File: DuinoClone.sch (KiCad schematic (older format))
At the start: 13 parts

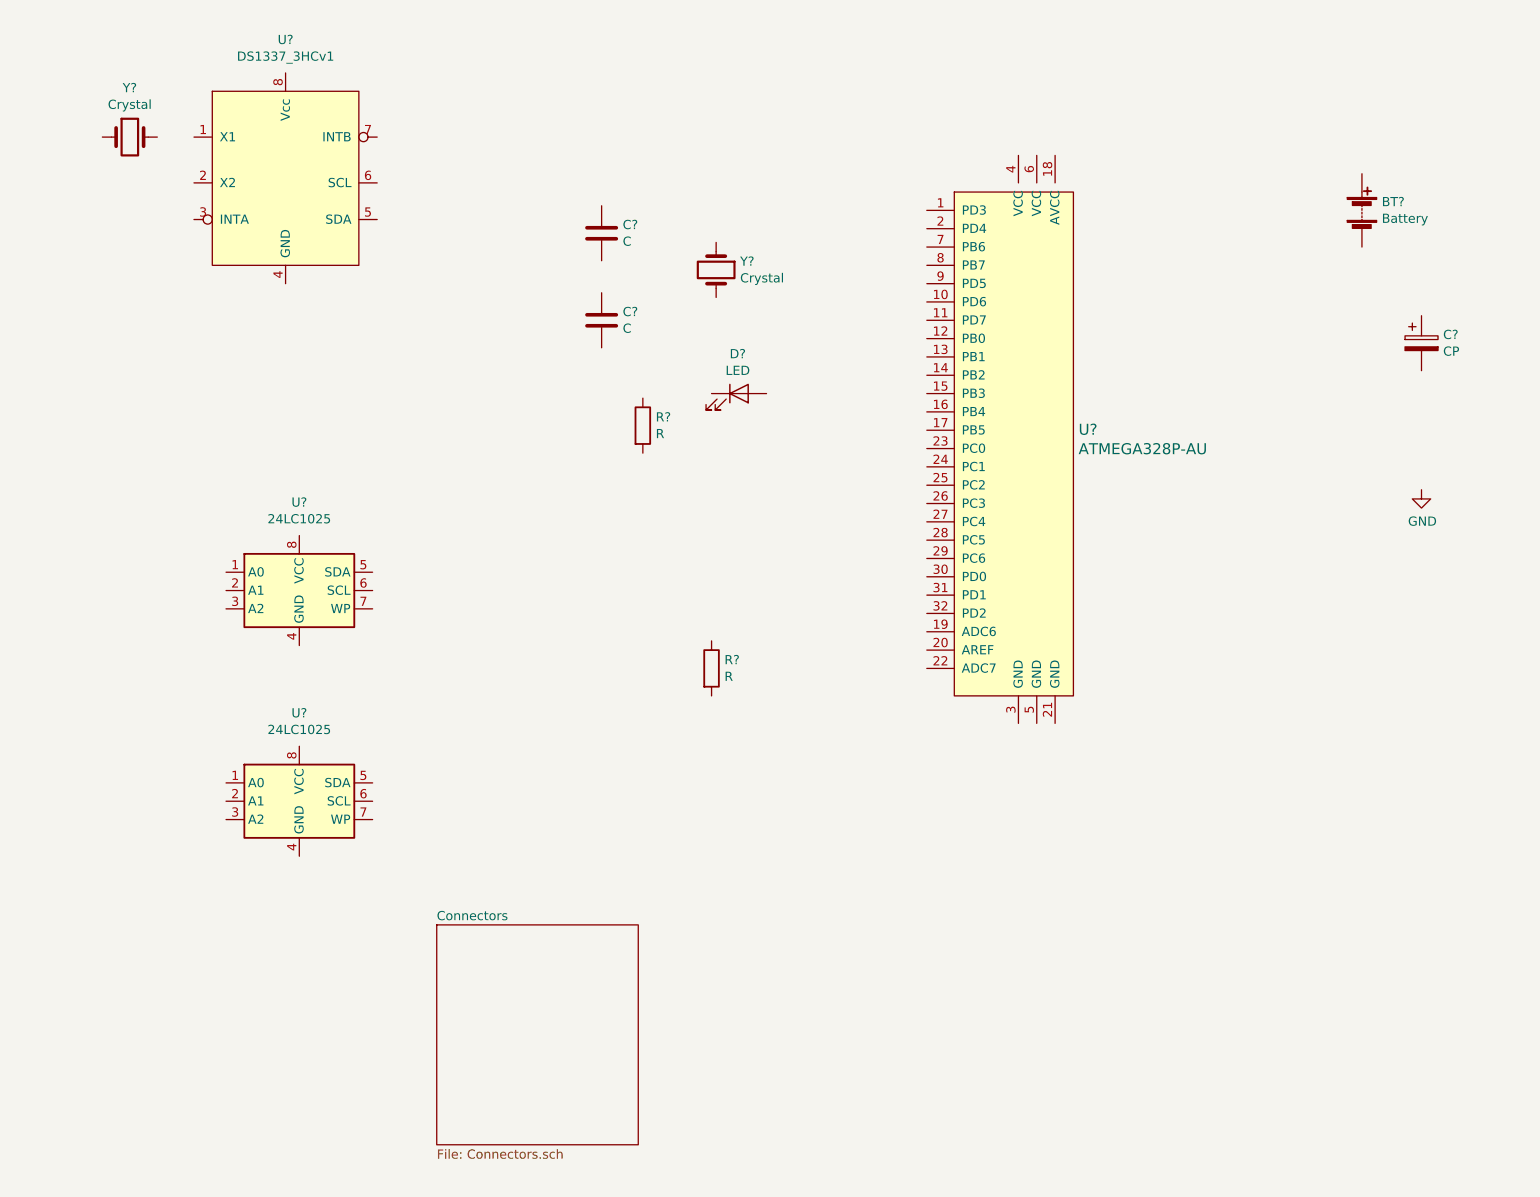
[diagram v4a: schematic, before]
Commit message: Completed associations and added component values
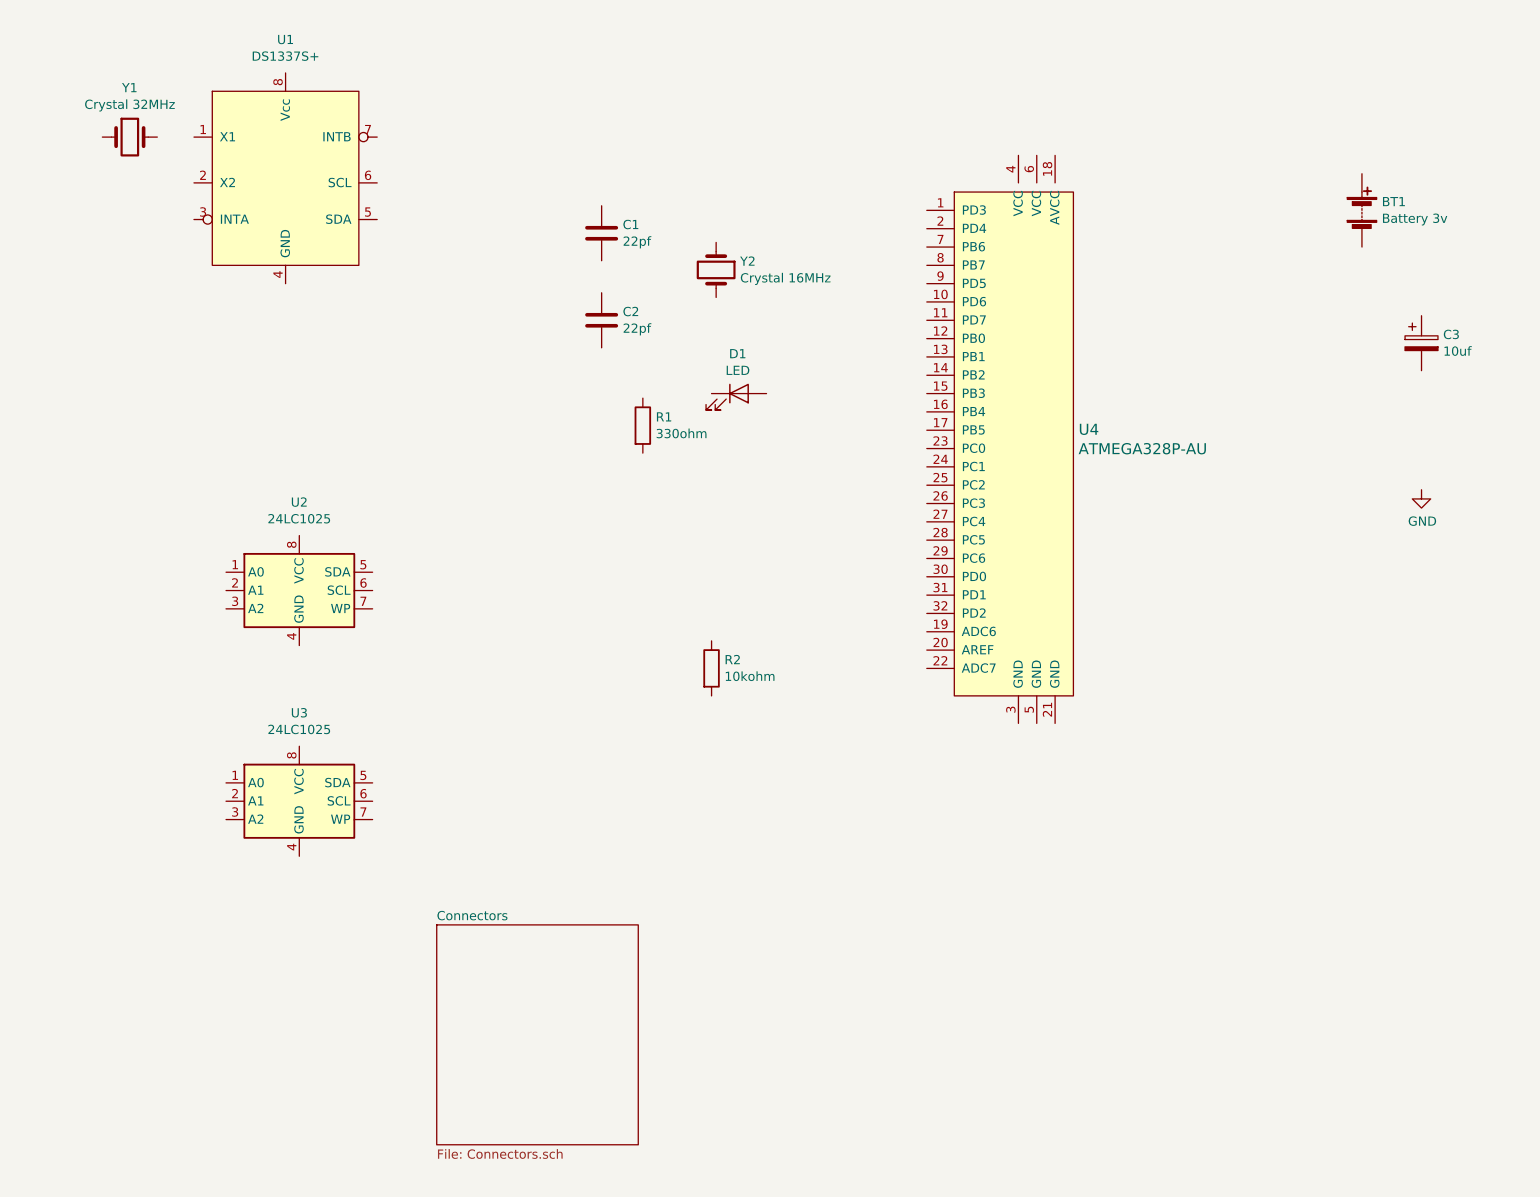
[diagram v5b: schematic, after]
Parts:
- BT1: renamed from BT?; value Battery -> Battery 3v; footprint (none) -> Connector_PinHeader_2.54mm:PinHeader_1x02_P2.54mm_Vertical
- C1, C2: renamed from C?; value C -> 22pf; footprint (none) -> Capacitor_SMD:C_0805_2012Metric_Pad1.15x1.40mm_HandSolder
- C3: renamed from C?; value CP -> 10uf; footprint (none) -> Capacitor_SMD:C_0805_2012Metric_Pad1.15x1.40mm_HandSolder
- D1: renamed from D?; footprint (none) -> LED_SMD:LED_0805_2012Metric_Pad1.15x1.40mm_HandSolder
- R1: renamed from R?; value R -> 330ohm; footprint (none) -> Resistor_SMD:R_0805_2012Metric_Pad1.15x1.40mm_HandSolder
- R2: renamed from R?; value R -> 10kohm; footprint (none) -> Resistor_SMD:R_0805_2012Metric_Pad1.15x1.40mm_HandSolder
- U1: renamed from U?; value DS1337_3HCv1 -> DS1337S+; footprint (none) -> Package_SO:SO-8_5.3x6.2mm_P1.27mm
- U2, U3: renamed from U?; footprint (none) -> Package_SO:SOIJ-8_5.3x5.3mm_P1.27mm
- Y1: renamed from Y?; value Crystal -> Crystal 32MHz; footprint (none) -> Crystal:Crystal_SMD_MicroCrystal_CC7V-T1A-2Pin_3.2x1.5mm_HandSoldering
- Y2: renamed from Y?; value Crystal -> Crystal 16MHz; footprint (none) -> Crystal:Crystal_SMD_5032-2Pin_5.0x3.2mm_HandSoldering
- gave numbers to parts that had none: 1
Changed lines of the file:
@@
 $EndDescr
 $Comp
-L Device:Battery BT?
+L Device:Battery BT1
 U 1 1 5CE2F41C
 P 8200 2275
-F 0 "BT?" H 8308 2321 50  0000 L CNN
-F 1 "Battery" H 8308 2230 50  0000 L CNN
-F 2 "" V 8200 2335 50  0001 C CNN
+F 0 "BT1" H 8308 2321 50  0000 L CNN
+F 1 "Battery 3v" H 8308 2230 50  0000 L CNN
+F 2 "Connector_PinHeader_2.54mm:PinHeader_1x02_P2.54mm_Vertical" V 8200 2335 50  0001 C CNN
 F 3 "~" V 8200 2335 50  0001 C CNN
 	1    8200 2275
@@
 $EndComp
 $Comp
-L Device:C C?
+L Device:C C1
 U 1 1 5CE30EAD
 P 4050 2400
-F 0 "C?" H 4165 2446 50  0000 L CNN
-F 1 "C" H 4165 2355 50  0000 L CNN
-F 2 "" H 4088 2250 50  0001 C CNN
+F 0 "C1" H 4165 2446 50  0000 L CNN
+F 1 "22pf" H 4165 2355 50  0000 L CNN
+F 2 "Capacitor_SMD:C_0805_2012Metric_Pad1.15x1.40mm_HandSolder" H 4088 2250 50  0001 C CNN
 F 3 "~" H 4050 2400 50  0001 C CNN
 	1    4050 2400
@@
 $EndComp
 $Comp
-L Device:C C?
+L Device:C C2
 U 1 1 5CE31ACC
 P 4050 2875
-F 0 "C?" H 4165 2921 50  0000 L CNN
-F 1 "C" H 4165 2830 50  0000 L CNN
-F 2 "" H 4088 2725 50  0001 C CNN
+F 0 "C2" H 4165 2921 50  0000 L CNN
+F 1 "22pf" H 4165 2830 50  0000 L CNN
+F 2 "Capacitor_SMD:C_0805_2012Metric_Pad1.15x1.40mm_HandSolder" H 4088 2725 50  0001 C CNN
 F 3 "~" H 4050 2875 50  0001 C CNN
 	1    4050 2875
@@
 $EndComp
 $Comp
-L Device:CP C?
+L Device:CP C3
 U 1 1 5CE322B6
 P 8525 3000
-F 0 "C?" H 8643 3046 50  0000 L CNN
-F 1 "CP" H 8643 2955 50  0000 L CNN
-F 2 "" H 8563 2850 50  0001 C CNN
+F 0 "C3" H 8643 3046 50  0000 L CNN
+F 1 "10uf" H 8643 2955 50  0000 L CNN
+F 2 "Capacitor_SMD:C_0805_2012Metric_Pad1.15x1.40mm_HandSolder" H 8563 2850 50  0001 C CNN
 F 3 "~" H 8525 3000 50  0001 C CNN
 	1    8525 3000
@@
 $EndComp
 $Comp
-L Device:LED D?
+L Device:LED D1
 U 1 1 5CE330B4
 P 4800 3275
-F 0 "D?" H 4793 3491 50  0000 C CNN
+F 0 "D1" H 4793 3491 50  0000 C CNN
 F 1 "LED" H 4793 3400 50  0000 C CNN
-F 2 "" H 4800 3275 50  0001 C CNN
+F 2 "LED_SMD:LED_0805_2012Metric_Pad1.15x1.40mm_HandSolder" H 4800 3275 50  0001 C CNN
 F 3 "~" H 4800 3275 50  0001 C CNN
 	1    4800 3275
@@
 $EndComp
 $Comp
-L Device:R R?
+L Device:R R1
 U 1 1 5CE33F79
 P 4275 3450
-F 0 "R?" H 4345 3496 50  0000 L CNN
-F 1 "R" H 4345 3405 50  0000 L CNN
-F 2 "" V 4205 3450 50  0001 C CNN
+F 0 "R1" H 4345 3496 50  0000 L CNN
+F 1 "330ohm" H 4345 3405 50  0000 L CNN
+F 2 "Resistor_SMD:R_0805_2012Metric_Pad1.15x1.40mm_HandSolder" V 4205 3450 50  0001 C CNN
 F 3 "~" H 4275 3450 50  0001 C CNN
 	1    4275 3450
@@
 $EndComp
 $Comp
-L Device:R R?
+L Device:R R2
 U 1 1 5CE34AF5
 P 4650 4775
-F 0 "R?" H 4720 4821 50  0000 L CNN
-F 1 "R" H 4720 4730 50  0000 L CNN
-F 2 "" V 4580 4775 50  0001 C CNN
+F 0 "R2" H 4720 4821 50  0000 L CNN
+F 1 "10kohm" H 4720 4730 50  0000 L CNN
+F 2 "Resistor_SMD:R_0805_2012Metric_Pad1.15x1.40mm_HandSolder" V 4580 4775 50  0001 C CNN
 F 3 "~" H 4650 4775 50  0001 C CNN
 	1    4650 4775
@@
 $EndComp
 $Comp
-L Memory_EEPROM:24LC1025 U?
+L Memory_EEPROM:24LC1025 U2
 U 1 1 5CE35387
 P 2400 4350
-F 0 "U?" H 2400 4831 50  0000 C CNN
+F 0 "U2" H 2400 4831 50  0000 C CNN
 F 1 "24LC1025" H 2400 4740 50  0000 C CNN
-F 2 "" H 2400 4350 50  0001 C CNN
+F 2 "Package_SO:SOIJ-8_5.3x5.3mm_P1.27mm" H 2400 4350 50  0001 C CNN
 F 3 "http://ww1.microchip.com/downloads/en/DeviceDoc/21941B.pdf" H 2400 4350 50  0001 C CNN
 	1    2400 4350
@@
 $EndSheet
 $Comp
-L dk_Embedded-Microcontrollers:ATMEGA328P-AU U?
+L dk_Embedded-Microcontrollers:ATMEGA328P-AU U4
 U 1 1 5CE4135D
 P 6325 3575
-F 0 "U?" H 6653 3678 60  0000 L CNN
+F 0 "U4" H 6653 3678 60  0000 L CNN
 F 1 "ATMEGA328P-AU" H 6653 3572 60  0000 L CNN
 F 2 "digikey-footprints:TQFP-32_7x7mm" H 6525 3775 60  0001 L CNN
@@
 $EndComp
 $Comp
-L DuinoClone:DS1337_3HCv1 U?
+L DuinoClone:DS1337_3HCv1 U1
 U 1 1 5CE464AF
 P 2325 2075
-F 0 "U?" H 2325 2806 50  0000 C CNN
-F 1 "DS1337_3HCv1" H 2325 2715 50  0000 C CNN
-F 2 "" H 2675 2625 50  0001 C CNN
+F 0 "U1" H 2325 2806 50  0000 C CNN
+F 1 "DS1337S+" H 2325 2715 50  0000 C CNN
+F 2 "Package_SO:SO-8_5.3x6.2mm_P1.27mm" H 2675 2625 50  0001 C CNN
 F 3 "http://www.farnell.com/datasheets/74348.pdf" H 2675 2625 50  0001 C CNN
 	1    2325 2075
@@
 $EndComp
 $Comp
-L Device:Crystal Y?
+L Device:Crystal Y1
 U 1 1 5CE47483
 P 1475 1875
-F 0 "Y?" H 1475 2143 50  0000 C CNN
-F 1 "Crystal" H 1475 2052 50  0000 C CNN
-F 2 "" H 1475 1875 50  0001 C CNN
+F 0 "Y1" H 1475 2143 50  0000 C CNN
+F 1 "Crystal 32MHz" H 1475 2052 50  0000 C CNN
+F 2 "Crystal:Crystal_SMD_MicroCrystal_CC7V-T1A-2Pin_3.2x1.5mm_HandSoldering" H 1475 1875 50  0001 C CNN
 F 3 "~" H 1475 1875 50  0001 C CNN
 	1    1475 1875
@@
 $EndComp
 $Comp
-L Device:Crystal Y?
+L Device:Crystal Y2
 U 1 1 5CE4858A
 P 4675 2600
-F 0 "Y?" V 4629 2731 50  0000 L CNN
-F 1 "Crystal" V 4720 2731 50  0000 L CNN
-F 2 "" H 4675 2600 50  0001 C CNN
+F 0 "Y2" V 4629 2731 50  0000 L CNN
+F 1 "Crystal 16MHz" V 4720 2731 50  0000 L CNN
+F 2 "Crystal:Crystal_SMD_5032-2Pin_5.0x3.2mm_HandSoldering" H 4675 2600 50  0001 C CNN
 F 3 "~" H 4675 2600 50  0001 C CNN
 	1    4675 2600
@@
 $EndComp
 $Comp
-L Memory_EEPROM:24LC1025 U?
+L Memory_EEPROM:24LC1025 U3
 U 1 1 5CE55027
 P 2400 5500
-F 0 "U?" H 2400 5981 50  0000 C CNN
+F 0 "U3" H 2400 5981 50  0000 C CNN
 F 1 "24LC1025" H 2400 5890 50  0000 C CNN
-F 2 "" H 2400 5500 50  0001 C CNN
+F 2 "Package_SO:SOIJ-8_5.3x5.3mm_P1.27mm" H 2400 5500 50  0001 C CNN
 F 3 "http://ww1.microchip.com/downloads/en/DeviceDoc/21941B.pdf" H 2400 5500 50  0001 C CNN
 	1    2400 5500
@@
 $EndComp
 $Comp
-L power:GND #PWR?
+L power:GND #PWR01
 U 1 1 5CE63FB2
 P 8525 3800
-F 0 "#PWR?" H 8525 3550 50  0001 C CNN
+F 0 "#PWR01" H 8525 3550 50  0001 C CNN
 F 1 "GND" H 8530 3627 50  0000 C CNN
 F 2 "" H 8525 3800 50  0001 C CNN

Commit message: Finished the hiearchical labels and pins
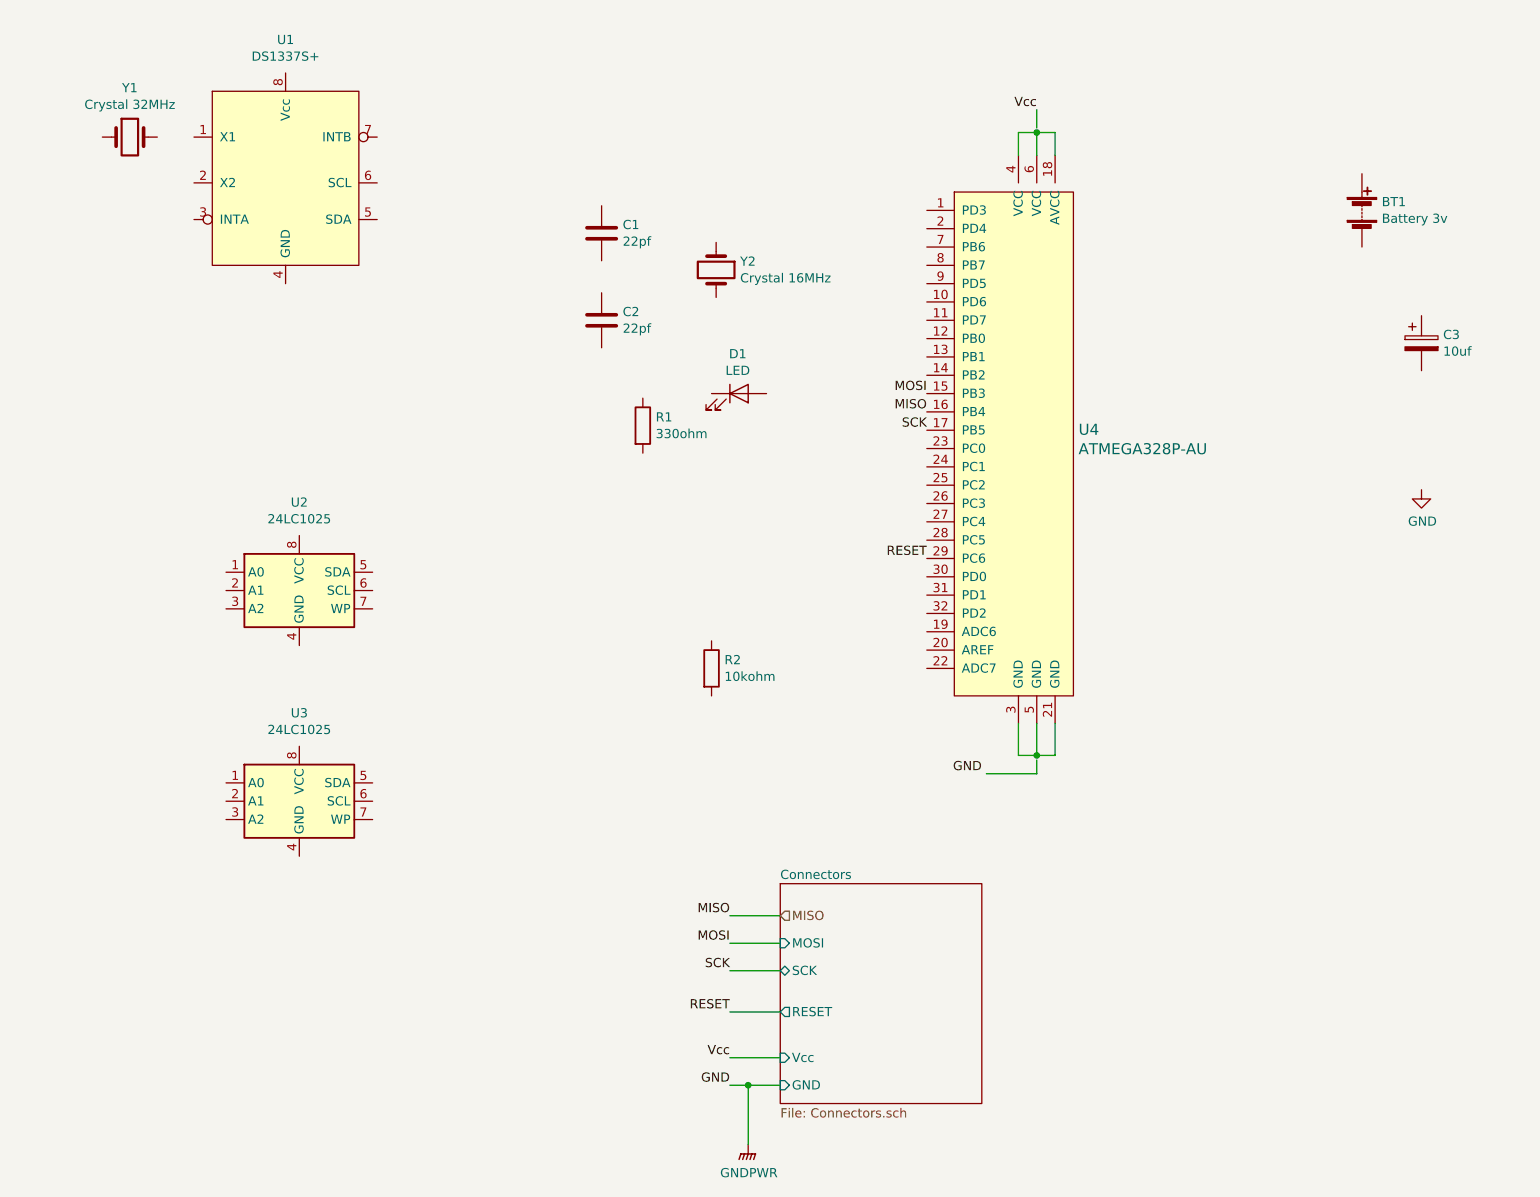
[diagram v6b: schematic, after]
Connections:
- net labels added: GNDPWR, MISO, MOSI, RESET, SCK, Vcc
- wire segments 0 -> 21
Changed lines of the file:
@@
 	1    0    0    -1
 $EndComp
-$Sheet
-S 3150 6175 1100 1200
-U 5CE3C2E7
-F0 "Connectors" 50
-F1 "Connectors.sch" 50
-$EndSheet
 $Comp
 L dk_Embedded-Microcontrollers:ATMEGA328P-AU U4
@@
 	1    0    0    -1
 $EndComp
+Text HLabel 5025 6125 2    50   Input ~ 0
+MISO
+Text Label 4750 6125 2    50   ~ 0
+MISO
+Text Label 5825 3375 2    50   ~ 0
+MISO
+$Sheet
+S 5025 5950 1100 1200
+U 5CE3C2E7
+F0 "Connectors" 50
+F1 "Connectors.sch" 50
+F2 "SCK" B L 5025 6425 50
+F3 "RESET" O L 5025 6650 50
+F4 "Vcc" I L 5025 6900 50
+F5 "MOSI" I L 5025 6275 50
+F6 "GND" I L 5025 7050 50
+$EndSheet
+Text Label 4750 6425 2    50   ~ 0
+SCK
+Text Label 4750 6650 2    50   ~ 0
+RESET
+Text Label 4750 6900 2    50   ~ 0
+Vcc
+Text Label 4750 6275 2    50   ~ 0
+MOSI
+Text Label 4750 7050 2    50   ~ 0
+GND
+Wire Wire Line
+	4750 6125 5025 6125
+Wire Wire Line
+	4750 6275 5025 6275
+Wire Wire Line
+	4750 6425 5025 6425
+Wire Wire Line
+	4750 6650 5025 6650
+Wire Wire Line
+	4750 6900 5025 6900
+Wire Wire Line
+	4750 7050 4850 7050
+Text Label 5825 3275 2    50   ~ 0
+MOSI
+Text Label 5825 3475 2    50   ~ 0
+SCK
+Text Label 5825 4175 2    50   ~ 0
+RESET
+Text Label 6425 1725 2    50   ~ 0
+Vcc
+Wire Wire Line
+	6325 1975 6325 1850
+Wire Wire Line
+	6325 1850 6425 1850
+Wire Wire Line
+	6525 1850 6525 1975
+Wire Wire Line
+	6425 1975 6425 1850
+Connection ~ 6425 1850
+Wire Wire Line
+	6425 1850 6525 1850
+Wire Wire Line
+	6425 1725 6425 1825
+Text Label 6125 5350 2    50   ~ 0
+GND
+Wire Wire Line
+	6325 5075 6325 5250
+Wire Wire Line
+	6325 5250 6425 5250
+Wire Wire Line
+	6525 5250 6525 5075
+Wire Wire Line
+	6425 5075 6425 5250
+Connection ~ 6425 5250
+Wire Wire Line
+	6425 5250 6525 5250
+Wire Wire Line
+	6150 5350 6425 5350
+Wire Wire Line
+	6425 5350 6425 5275
+$Comp
+L power:GNDPWR #PWR?
+U 1 1 5CE88593
+P 4850 7375
+F 0 "#PWR?" H 4850 7175 50  0001 C CNN
+F 1 "GNDPWR" H 4854 7221 50  0000 C CNN
+F 2 "" H 4850 7325 50  0001 C CNN
+F 3 "" H 4850 7325 50  0001 C CNN
+	1    4850 7375
+	1    0    0    -1
+$EndComp
+Wire Wire Line
+	4850 7375 4850 7050
+Connection ~ 4850 7050
+Wire Wire Line
+	4850 7050 5025 7050
 $EndSCHEMATC
